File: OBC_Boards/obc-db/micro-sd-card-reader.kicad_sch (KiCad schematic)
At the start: 6 parts, among them J6 ST11S008V4HR2000

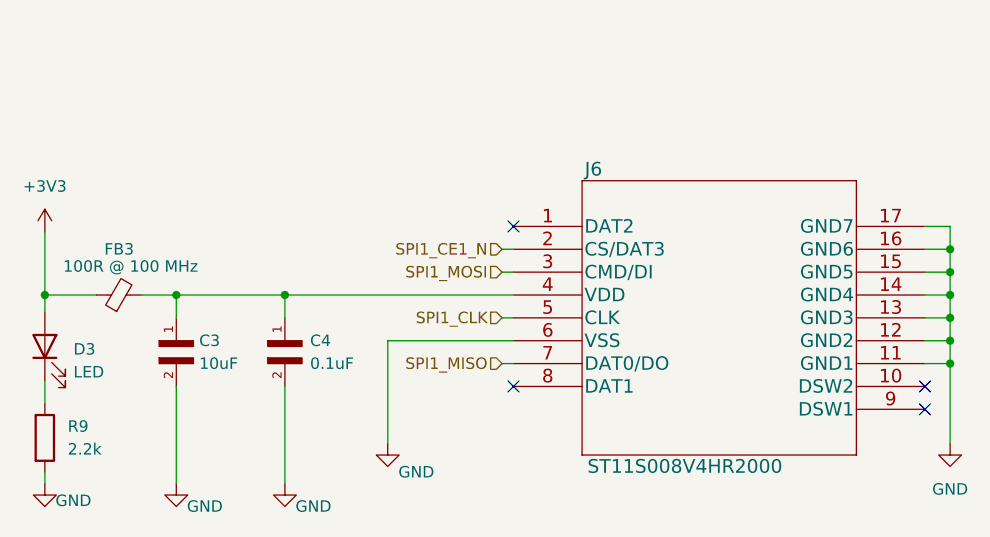
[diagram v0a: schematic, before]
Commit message: new microSD connector
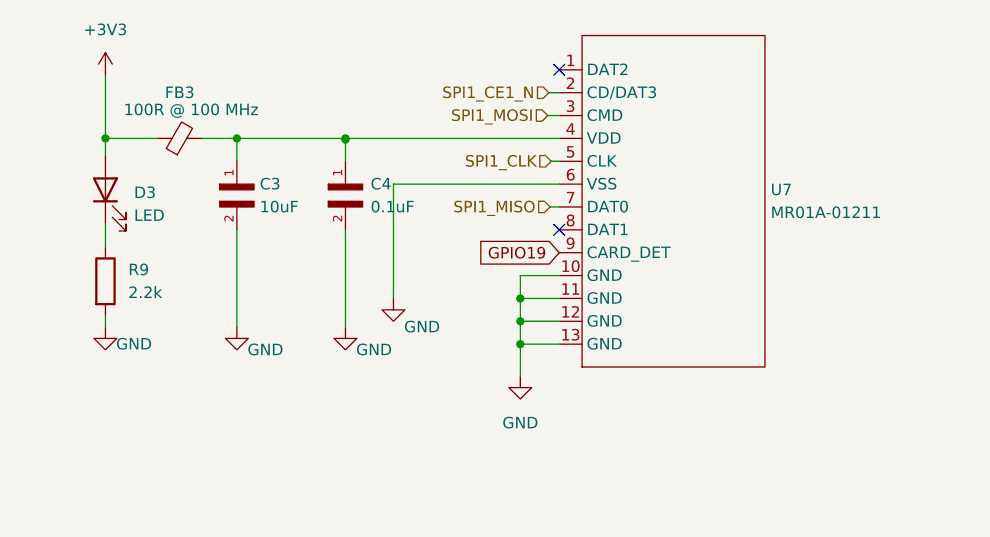
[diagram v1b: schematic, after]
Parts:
- removed J6: ST11S008V4HR2000, qset-footprints:ST11S008V4HR2000, symbol Buffer:ST11S008V4HR2000
- added U7: MR01A-01211, qset-footprints:MR01A-01211, symbol Imported_OBC_Library:MR01A-01211
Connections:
- net GND: now also U7.10 (GND), U7.11 (GND), U7.12 (GND), U7.13 (GND), U7.6 (VSS)
- net SPI1_CE1_N: now also U7.2 (CD/DAT3)
- net SPI1_CLK: now also U7.5 (CLK)
- net SPI1_MISO: now also U7.7 (DAT0)
- net SPI1_MOSI: now also U7.3 (CMD)
- net at C3.1, C4.1, FB3.2: now also U7.4 (VDD)
- new net GPIO19: U7.9 (CARD_DET)
- no-connect marks 4 -> 2
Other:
- moved on the sheet: C3, C4, D3, FB3, R9
